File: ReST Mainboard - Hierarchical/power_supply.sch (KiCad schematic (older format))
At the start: 22 parts, among them U3 ACT4088, U4 SC4626

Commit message: Mostly finished with main PCB. Only need to work the High Current Stuff out. On Vacation for now
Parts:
- added F3: F_Small, ReST-Library:FUSE-1812, symbol F_Small
- added F4: F_Small, Resistors_SMD:R_0805_HandSoldering, symbol F_Small
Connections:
- net +3V3: now also F4.1; no longer C33.1, L3.2, U4.4 (VOUT)
- net VEE: now also F3.1; no longer C12.1, L2.2, R7.2
- new net: C33.1, F4.2, L3.2, U4.4 (VOUT)
- new net: C12.1, F3.2, L2.2, R7.2
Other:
- moved on the sheet: C10, C11, C12, C32, C33, D2, L2, L3, R6, R7, U3, U4

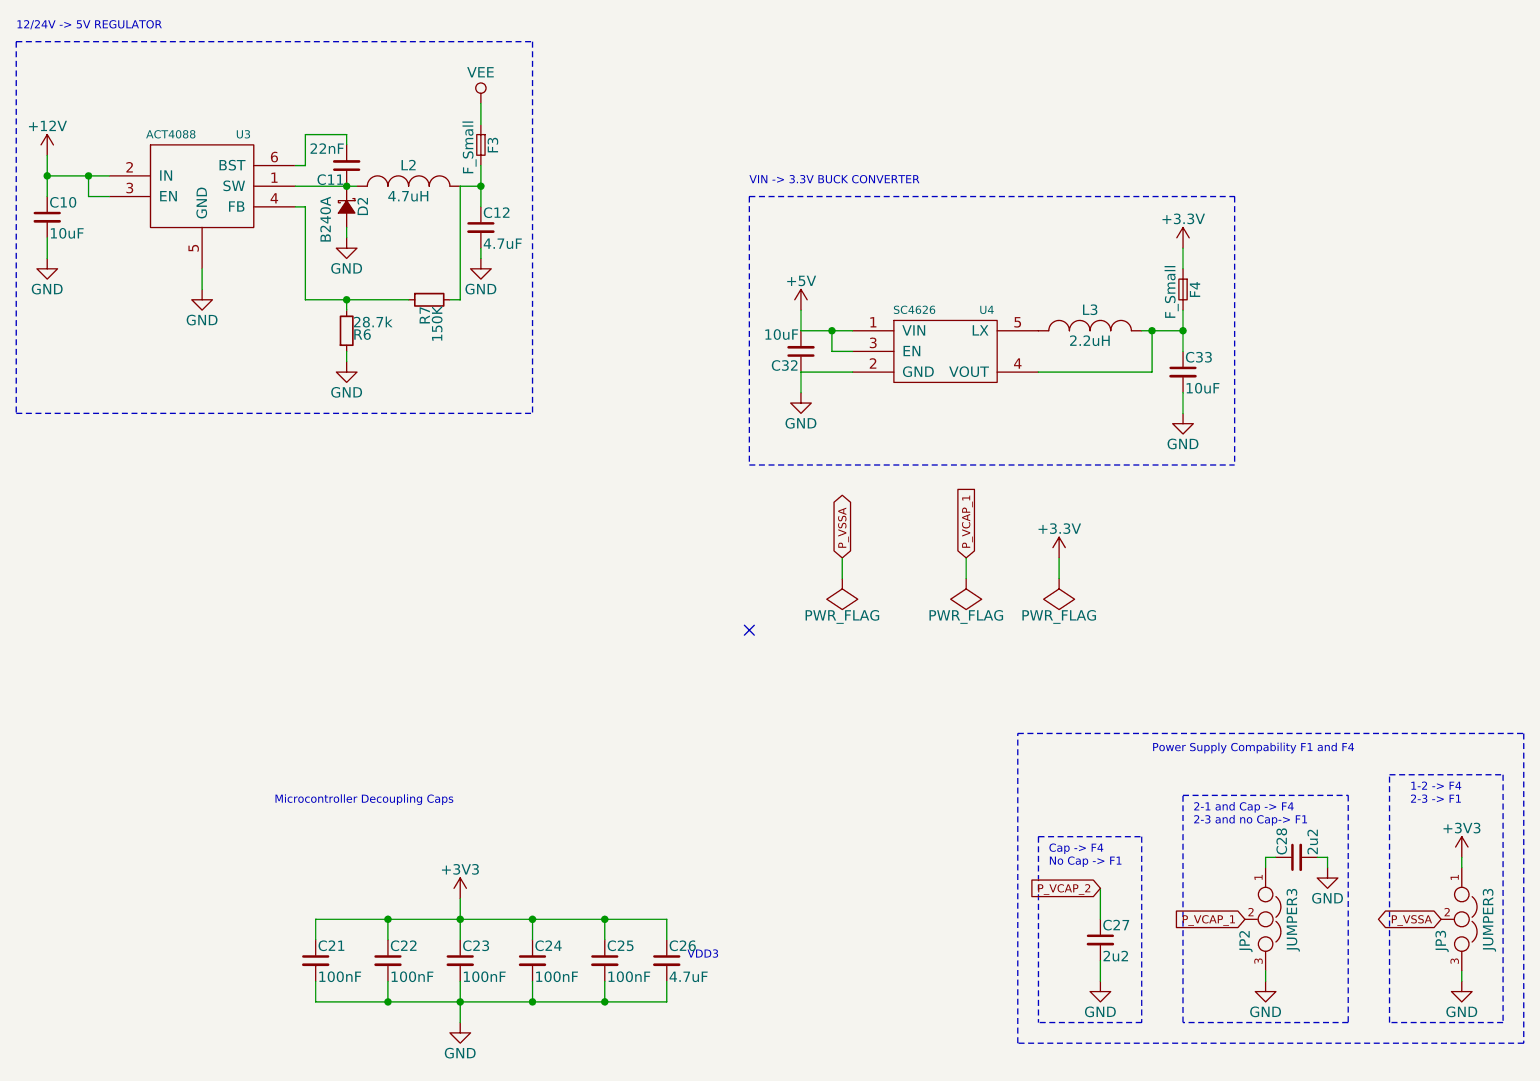
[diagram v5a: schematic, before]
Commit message: changed extra output circuit, removed 3.3V Buck and replaced with LDO
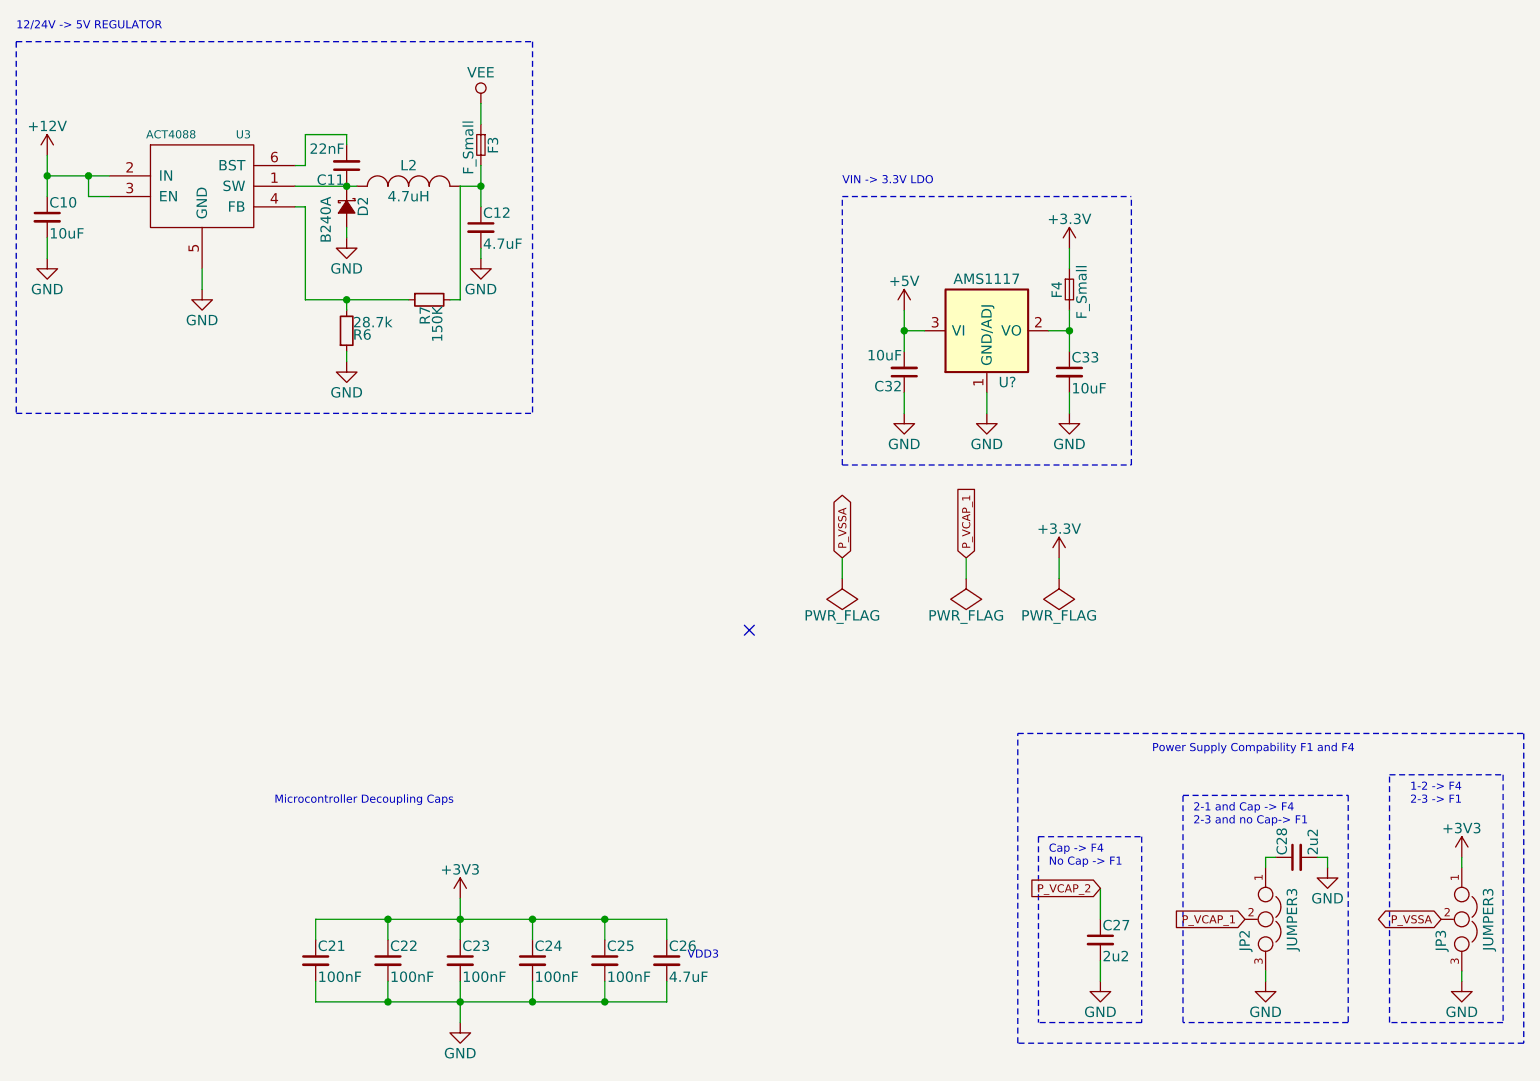
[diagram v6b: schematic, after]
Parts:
- removed L3: 2.2uH, ReST-Library:CD32, symbol INDUCTOR_SMALL
- removed U4: SC4626, TO_SOT_Packages_SMD:SOT-23-5, symbol SC4626
- added U?: AMS1117, TO_SOT_Packages_SMD:SOT-223, symbol AP1117
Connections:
- net +5V: now also U?.3 (VI)
- net GND: now also U?.1 (GND/ADJ)
- net at C33.1, F4.2: now also U?.2 (VO), U?.4 (VO)
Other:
- note added: "VIN -> 3.3V LDO"
- note removed: "VIN -> 3.3V BUCK CONVERTER"
- moved on the sheet: C32, C33, F4
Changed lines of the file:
@@
 Comment4 ""
 $EndDescr
-Text Notes 6100 2000 0    39   ~ 0
-VIN -> 3.3V BUCK CONVERTER
+Text Notes 6550 2000 0    39   ~ 0
+VIN -> 3.3V LDO
 $Comp
 L +3.3V #PWR0162
 U 1 1 576F5C64
-P 8200 2300
-F 0 "#PWR0162" H 8200 2150 50  0001 C CNN
-F 1 "+3.3V" H 8200 2440 50  0000 C CNN
-F 2 "" H 8200 2300 50  0000 C CNN
-F 3 "" H 8200 2300 50  0000 C CNN
-	1    8200 2300
-	1    0    0    -1
-$EndComp
-$Comp
-L INDUCTOR_SMALL L3
-U 1 1 576F5C6A
-P 7750 2700
-F 0 "L3" H 7750 2800 50  0000 C CNN
-F 1 "2.2uH" H 7750 2650 50  0000 C CNN
-F 2 "ReST-Library:CD32" H 7750 2700 50  0001 C CNN
-F 3 "" H 7750 2700 50  0000 C CNN
-	1    7750 2700
+P 7650 2300
+F 0 "#PWR0162" H 7650 2150 50  0001 C CNN
+F 1 "+3.3V" H 7650 2440 50  0000 C CNN
+F 2 "" H 7650 2300 50  0000 C CNN
+F 3 "" H 7650 2300 50  0000 C CNN
+	1    7650 2300
 	1    0    0    -1
 $EndComp
@@
 L GND #PWR0163
 U 1 1 576F5C71
-P 8200 3100
-F 0 "#PWR0163" H 8200 2850 50  0001 C CNN
-F 1 "GND" H 8200 2950 50  0000 C CNN
-F 2 "" H 8200 3100 50  0000 C CNN
-F 3 "" H 8200 3100 50  0000 C CNN
-	1    8200 3100
+P 7650 3100
+F 0 "#PWR0163" H 7650 2850 50  0001 C CNN
+F 1 "GND" H 7650 2950 50  0000 C CNN
+F 2 "" H 7650 3100 50  0000 C CNN
+F 3 "" H 7650 3100 50  0000 C CNN
+	1    7650 3100
 	1    0    0    -1
 $EndComp
@@
 L GND #PWR0164
 U 1 1 576F5C77
-P 6350 3000
-F 0 "#PWR0164" H 6350 2750 50  0001 C CNN
-F 1 "GND" H 6350 2850 50  0000 C CNN
-F 2 "" H 6350 3000 50  0000 C CNN
-F 3 "" H 6350 3000 50  0000 C CNN
-	1    6350 3000
-	1    0    0    -1
-$EndComp
-$Comp
-L SC4626 U4
-U 1 1 576F5C83
-P 7050 2800
-F 0 "U4" H 7250 3000 39  0000 C CNN
-F 1 "SC4626" H 6900 3000 39  0000 C CNN
-F 2 "TO_SOT_Packages_SMD:SOT-23-5" H 7050 2800 39  0001 C CNN
-F 3 "" H 7050 2800 39  0000 C CNN
-	1    7050 2800
+P 6850 3100
+F 0 "#PWR0164" H 6850 2850 50  0001 C CNN
+F 1 "GND" H 6850 2950 50  0000 C CNN
+F 2 "" H 6850 3100 50  0000 C CNN
+F 3 "" H 6850 3100 50  0000 C CNN
+	1    6850 3100
 	1    0    0    -1
 $EndComp
@@
 L C_Small C33
 U 1 1 576F5C8A
-P 8200 2900
-F 0 "C33" H 8210 2970 50  0000 L CNN
-F 1 "10uF" H 8210 2820 50  0000 L CNN
-F 2 "Capacitors_SMD:C_0805_HandSoldering" H 8200 2900 50  0001 C CNN
-F 3 "" H 8200 2900 50  0000 C CNN
-	1    8200 2900
-	1    0    0    -1
-$EndComp
-Wire Wire Line
-	8000 2700 8200 2700
-Wire Wire Line
-	7500 2900 8050 2900
-Wire Wire Line
-	8050 2900 8050 2700
-Connection ~ 8050 2700
-Wire Wire Line
-	8200 2600 8200 2800
-Connection ~ 8200 2700
-Wire Wire Line
-	8200 3100 8200 3000
+P 7650 2900
+F 0 "C33" H 7660 2970 50  0000 L CNN
+F 1 "10uF" H 7660 2820 50  0000 L CNN
+F 2 "Capacitors_SMD:C_0805_HandSoldering" H 7650 2900 50  0001 C CNN
+F 3 "" H 7650 2900 50  0000 C CNN
+	1    7650 2900
+	1    0    0    -1
+$EndComp
+Wire Wire Line
+	7650 2600 7650 2800
+Connection ~ 7650 2700
+Wire Wire Line
+	7650 3100 7650 3000
 $Comp
 L C_Small C32
 U 1 1 576F5C98
-P 6350 2800
-F 0 "C32" H 6360 2870 50  0000 L CNN
-F 1 "10uF" H 6360 2720 50  0000 L CNN
-F 2 "Capacitors_SMD:C_0805_HandSoldering" H 6350 2800 50  0001 C CNN
-F 3 "" H 6350 2800 50  0000 C CNN
-	1    6350 2800
+P 6850 2900
+F 0 "C32" H 6860 2970 50  0000 L CNN
+F 1 "10uF" H 6860 2820 50  0000 L CNN
+F 2 "Capacitors_SMD:C_0805_HandSoldering" H 6850 2900 50  0001 C CNN
+F 3 "" H 6850 2900 50  0000 C CNN
+	1    6850 2900
 	-1   0    0    1
 $EndComp
 Wire Wire Line
-	6600 2700 6350 2700
-Wire Wire Line
-	6350 2700 6350 2600
-Wire Wire Line
-	6600 2900 6350 2900
-Wire Wire Line
-	6600 2800 6500 2800
-Wire Wire Line
-	6500 2800 6500 2700
-Connection ~ 6500 2700
-Wire Wire Line
-	6350 2900 6350 3000
-Wire Notes Line
-	6100 2050 8450 2050
-Wire Notes Line
-	8450 2050 8450 3350
-Wire Notes Line
-	6100 2050 6100 3350
+	6850 2800 6850 2600
+Wire Wire Line
+	6850 3000 6850 3100
 $Comp
 L +5V #PWR0165
 U 1 1 576F5C7D
-P 6350 2600
-F 0 "#PWR0165" H 6350 2450 50  0001 C CNN
-F 1 "+5V" H 6350 2740 50  0000 C CNN
-F 2 "" H 6350 2600 50  0000 C CNN
-F 3 "" H 6350 2600 50  0000 C CNN
-	1    6350 2600
+P 6850 2600
+F 0 "#PWR0165" H 6850 2450 50  0001 C CNN
+F 1 "+5V" H 6850 2740 50  0000 C CNN
+F 2 "" H 6850 2600 50  0000 C CNN
+F 3 "" H 6850 2600 50  0000 C CNN
+	1    6850 2600
 	1    0    0    -1
 $EndComp
@@
 $EndComp
 Wire Wire Line
-	3000 1950 2700 1950
+	2700 1950 3000 1950
 Wire Wire Line
 	2700 1850 2700 2050
@@
 L F_Small F4
 U 1 1 5781A1A6
-P 8200 2500
-F 0 "F4" H 8160 2560 50  0000 L CNN
-F 1 "F_Small" H 8080 2440 50  0000 L CNN
-F 2 "Resistors_SMD:R_0805_HandSoldering" H 8200 2500 50  0001 C CNN
-F 3 "" H 8200 2500 50  0000 C CNN
-	1    8200 2500
-	0    1    1    0
-$EndComp
-Wire Wire Line
-	8200 2400 8200 2300
-Wire Notes Line
-	6100 3350 8450 3350
+P 7650 2500
+F 0 "F4" H 7610 2560 50  0000 L CNN
+F 1 "F_Small" H 7530 2440 50  0000 L CNN
+F 2 "Resistors_SMD:R_0805_HandSoldering" H 7650 2500 50  0001 C CNN
+F 3 "" H 7650 2500 50  0000 C CNN
+	1    7650 2500
+	0    -1   1    0
+$EndComp
+Wire Wire Line
+	7650 2400 7650 2300
 $Comp
 L F_Small F3
@@
 Wire Wire Line
 	7600 3800 7600 3900
+$Comp
+L AP1117 U?
+U 1 1 57E5CCE8
+P 7250 2700
+F 0 "U?" H 7350 2450 50  0000 C CNN
+F 1 "AMS1117" H 7250 2950 50  0000 C CNN
+F 2 "TO_SOT_Packages_SMD:SOT-223" H 7250 2350 50  0001 C CNN
+F 3 "" H 7350 2450 50  0000 C CNN
+	1    7250 2700
+	1    0    0    -1
+$EndComp
+Wire Wire Line
+	6850 2700 6950 2700
+Connection ~ 6850 2700
+$Comp
+L GND #PWR?
+U 1 1 57E5D47C
+P 7250 3100
+F 0 "#PWR?" H 7250 2850 50  0001 C CNN
+F 1 "GND" H 7250 2950 50  0000 C CNN
+F 2 "" H 7250 3100 50  0000 C CNN
+F 3 "" H 7250 3100 50  0000 C CNN
+	1    7250 3100
+	1    0    0    -1
+$EndComp
+Wire Wire Line
+	7250 3100 7250 3000
+Wire Wire Line
+	7550 2700 7650 2700
+Wire Notes Line
+	6550 3350 6550 2050
+Wire Notes Line
+	6550 2050 7950 2050
+Wire Notes Line
+	6550 3350 7950 3350
+Wire Notes Line
+	7950 3350 7950 2050
 $EndSCHEMATC

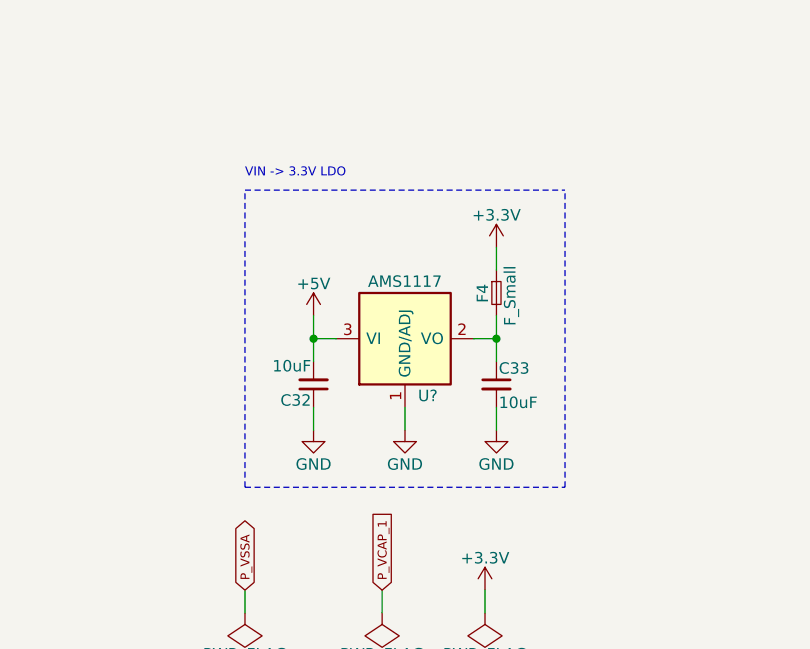
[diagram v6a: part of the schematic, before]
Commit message: changed 3.3V LDO due to symbol errors
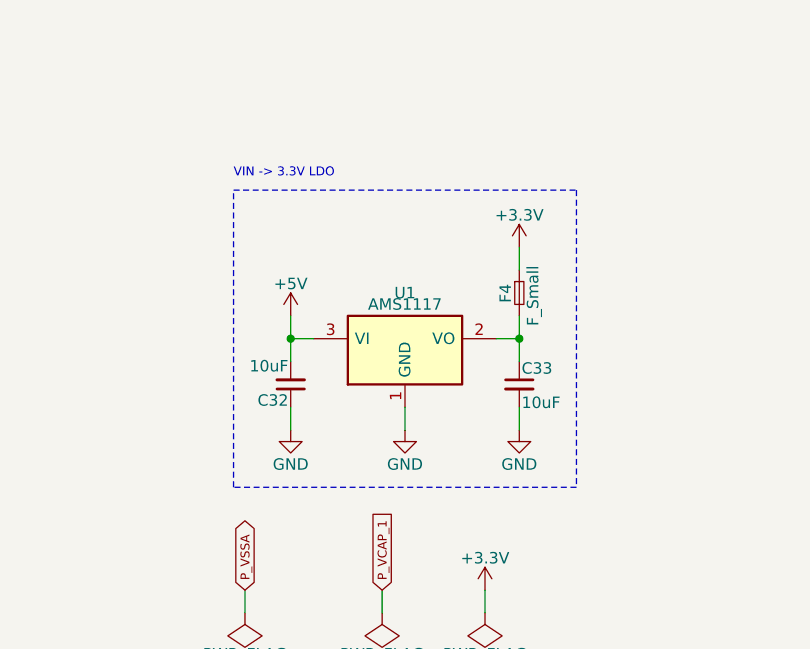
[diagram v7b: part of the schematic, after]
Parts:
- removed U?: AMS1117, TO_SOT_Packages_SMD:SOT-223, symbol AP1117
- added U1: AMS1117, TO_SOT_Packages_SMD:SOT-223, symbol LD1117S12CTR
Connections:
- net +5V: now also U1.3 (VI)
- net GND: now also U1.1 (GND)
- net at C33.1, F4.2: now also U1.2 (VO)
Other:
- moved on the sheet: C32, C33, F4
